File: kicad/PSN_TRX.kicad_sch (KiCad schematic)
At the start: 164 parts, among them IC1 LP2950L-5.0V, IC2 NJM2904, J1 PWR_IN, J2 PWR_IN, J3 PWR_IN, J4 MIC-IN, J5 FREQ-VC, J6 Volume, K1 G5V-2, Q1 3SK59, Q10 2SK439, Q11 2SC1815, Q12 2SC1815, Q13 2SC1815, Q14 2SK439, Q15 2SC1815, Q17 2SC1815, Q2 2SC1923, Q3 2SC1815, Q4 2SC1815, Q5 2SC2120, Q6 2SA950, Q7 2SC1923, Q8 2SC1923, Q9 2SK439, SW1 SW, SW2 SW, T1 ST-71, X1 50.5MHz/3

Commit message: Arduino Nano R4 移植 & KiCad ライブラリ統合
- Arduino Nano R4 (Renesas RA4M1) への移植完了
  * スケッチ: ESP32 → Nano R4 対応に変更
  * GPIO ピン: 再割り当て (GPIO21/22 → A4/A5 など)
  * ストレージ: Preferences → EEPROM に変更
  * リポジトリ名: PSN_TRX_ESP32 → PSN_TRX_Nano_R4

- KiCad シンボル・フットプリント作成
  * Arduino_Nano_R4_Socket (DIP 30)
  * Si5351A (QFN-20)
  * Si5351_DIP8 モジュール (DIP 8)
  * すべてピン位置を 2.54mm グリッドに整列

- ライブラリ統合
  * sym-lib-table に 4 つのシンボルライブラリ登録
  * fp-lib-table に フットプリント登録
  * 絶対パスに統一

- ドキュメント更新
  * PSN_TRX_VFO改造仕様書.docx に全変更内容を記録
  * ピン配置表、ライブラリ情報を追加

- VXO 回路変更
  * VXO 部分を別の回路に変更

Co-Authored-By: Claude Haiku 4.5 <noreply@anthropic.com>
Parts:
- removed C10, C9: 100p, Capacitor_THT:C_Disc_D3.0mm_W1.6mm_P2.50mm, symbol Device:C
- removed C11, C12, C14: 47p, Capacitor_THT:C_Disc_D3.0mm_W1.6mm_P2.50mm, symbol Device:C
- removed C112: 0.01u, Capacitor_THT:C_Disc_D5.0mm_W2.5mm_P2.50mm, symbol Device:C
- removed C13: 5p, Capacitor_THT:C_Disc_D3.0mm_W1.6mm_P2.50mm, symbol Device:C
- removed C18: 15p, Capacitor_THT:C_Disc_D3.0mm_W1.6mm_P2.50mm, symbol Device:C
- removed C19, C20: 33p, Capacitor_THT:C_Disc_D3.0mm_W1.6mm_P2.50mm, symbol Device:C
- removed J5: FREQ-VC, Connector_PinHeader_2.54mm:PinHeader_1x02_P2.54mm_Vertical, symbol Connector_Generic:Conn_01x02
- removed L3: 7T5, PSN_TRX:L_FCZ07S_CT, symbol PSN_TRX:L_7T50_CT
- removed L4: T-30-10 6T/0.4mm, PSN_TRX:L_T30_2pin_Vertical, symbol Device:L
- removed L5: T-30-10 6T+1T/0.4mm, PSN_TRX:L_T30_3pin_Vertical, symbol Device:Transformer_1P_1S
- removed L7: 7T50, PSN_TRX:L_FCZ07S_CT, symbol PSN_TRX:L_7T50_CT
- removed Q10: 2SK439, Package_TO_SOT_THT:TO-92_Inline, symbol Device:Q_NMOS
- removed Q7, Q8: 2SC1923, Package_TO_SOT_THT:TO-92_Inline, symbol Transistor_BJT:Q_NPN_BCE
- removed R16: 10k, Resistor_THT:R_Axial_DIN0207_L6.3mm_D2.5mm_P2.54mm_Vertical, symbol Device:R
- removed R17, R20: 100k, Resistor_THT:R_Axial_DIN0207_L6.3mm_D2.5mm_P2.54mm_Vertical, symbol Device:R
- removed R18: 1k, Resistor_THT:R_Axial_DIN0207_L6.3mm_D2.5mm_P2.54mm_Vertical, symbol Device:R
- removed R44: 100, Resistor_THT:R_Axial_DIN0207_L6.3mm_D2.5mm_P2.54mm_Vertical, symbol Device:R
- removed TC1, TC2: 40p, PSN_TRX:C_Trimmer_TMCV01, symbol Device:C_Variable
- removed VC1: 30p, PSN_TRX:C_Trimmer_TMCV01, symbol Device:C_Variable
- removed X1: 50.5MHz/3, Crystal:Crystal_HC49-4H_Vertical, symbol Device:Crystal
- added A1: Arduino_Nano_R4_Socket, PSN_TRX:Arduino_Nano_R4_Socket, symbol Arduino_Nano_R4:Arduino_Nano_R4_Socket
- added C128, C129, C130, C131: 47PF, Capacitor_THT:C_Disc_D5.0mm_W2.5mm_P2.50mm, symbol Device:C
- added L16, L17: 100nH, PSN_TRX:L_AL0510-153K_Vertical, symbol Device:L
- added U1: Si5351_DIP8, PSN_TRX:DIP-8_W7.62mm, symbol Si5351_DIP8:Si5351_DIP8
- added VR6, VR7: 500, Potentiometer_THT:Potentiometer_Alps_RK09K_Single_Vertical, symbol Device:R_Potentiometer
- R21: value 220k -> 47
- R34: value 100 -> 47
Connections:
- net +5V: now also A1.30 (VIN), U1.8 (VDD); no longer C115.1, R21.2
- net GND: now also R21.2, A1.18 (GND), A1.28 (GND), A1.29 (GND), C128.1, C129.1, C130.1, C131.1, U1.4 (GND); no longer C115.2, C116.2
- net at R21.1: now also C114.2, C21.1, VR6.1
- net at C116.1: now also C131.2, L17.1
- net at R34.1: now also C22.1, VR7.1; no longer C21.1
- new net: C115.1, C128.2, L16.1
- new net: C129.2, L16.2, VR6.2, VR6.3
- new net: C130.2, L17.2, VR7.2, VR7.3
- new net: C115.2, U1.5 (CLK0)
- new net: A1.21 (A5/SCL), U1.2 (SCL)
- new net: A1.22 (A4/SDA), U1.3 (SDA)
- new net: C116.2, U1.6 (CLK1)
- no-connect marks 9 -> 30
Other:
- note added: "DDS"
- note removed: "VXO"
- moved on the sheet: C1, C100, C101, C102, C103, C104, C105, C111, C113, C114, C117, C118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

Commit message: J5 I2C_OUT コネクタ（3ピン）を追加
- Arduino Nano R4 の A4（SDA）、A5（SCL）から I2C 出力コネクタを実装
- J5: 3ピンコネクタ（SDA/SCL/GND）
- フットプリント: Connector_PinHeader_2.54mm:PinHeader_1x03_P2.54mm_Vertical
- シンボル: PSN_TRX:I2C_OUT カスタムシンボル
- スケマティクスに配線完了

Co-Authored-By: Claude Haiku 4.5 <noreply@anthropic.com>
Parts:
- added J5: Conn_01x03_MountingPin, Connector_PinHeader_2.54mm:PinHeader_1x03_P2.54mm_Vertical, symbol Connector_Generic_MountingPin:Conn_01x03_MountingPin
- added J5: I2C_OUT, Connector_PinHeader_2.54mm:PinHeader_1x03_P2.54mm_Vertical, symbol PSN_TRX:I2C_OUT
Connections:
- net GND: now also J5.3 (Pin_3)
- net at A1.21 (A5/SCL), U1.2 (SCL): now also J5.2 (Pin_2)
- net at A1.22 (A4/SDA), U1.3 (SDA): now also J5.1 (Pin_1)

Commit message: スケマティクス更新（KiCad 再起動後の反映）
- J5 I2C_OUT シンボル表示を PSN_TRX:I2C_OUT に更新
- キャッシュクリア後の最終確認

Co-Authored-By: Claude Haiku 4.5 <noreply@anthropic.com>
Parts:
- removed J5: Conn_01x03_MountingPin, Connector_PinHeader_2.54mm:PinHeader_1x03_P2.54mm_Vertical, symbol Connector_Generic_MountingPin:Conn_01x03_MountingPin
- added J5: I2C_OUT, Connector_PinHeader_2.54mm:PinHeader_1x03_P2.54mm_Vertical, symbol PSN_TRX:I2C_OUT
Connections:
- net GND: now also J5.3 (GND)
- net at A1.22 (A4/SDA), U1.3 (SDA): now also J5.1 (SDA)
- net at A1.21 (A5/SCL), U1.2 (SCL): now also J5.2 (SCL)
- no-connect marks 30 -> 31
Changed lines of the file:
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@@
 	)
 	(no_connect
+		(at 690.88 318.77)
+	)
+	(no_connect
 		(at 671.83 336.55)
 	)
@@
 	)
 	(symbol
+		(lib_id "PSN_TRX:I2C_OUT")
+		(at 744.22 383.54 0)
+		(unit 1)
+		(body_style 1)
+		(exclude_from_sim no)
+		(in_bom yes)
+		(on_board yes)
+		(in_pos_files yes)
+		(dnp no)
+		(property "Reference" "J5"
+			(at 751.84 382.524 0)
+			(show_name no)
+			(do_not_autoplace no)
+			(effects
+				(font
+					(size 1.27 1.27)
+					(thickness 0.15)
+				)
+				(justify left)
+			)
+		)
+		(property "Value" "I2C_OUT"
+			(at 751.332 385.064 0)
+			(show_name no)
+			(do_not_autoplace no)
+			(effects
+				(font
+					(size 1.27 1.27)
+					(thickness 0.15)
+				)
+				(justify left)
+			)
+		)
+		(property "Footprint" "Connector_PinHeader_2.54mm:PinHeader_1x03_P2.54mm_Vertical"
+			(at 744.22 383.54 0)
+			(hide yes)
+			(show_name no)
+			(do_not_autoplace no)
+			(effects
+				(font
+					(size 1.27 1.27)
+					(thickness 0.15)
+				)
+			)
+		)
+		(property "Datasheet" ""
+			(at 744.22 383.54 0)
+			(hide yes)
+			(show_name no)
+			(do_not_autoplace no)
+			(effects
+				(font
+					(size 1.27 1.27)
+					(thickness 0.15)
+				)
+			)
+		)
+		(property "Description" "I2C output connector, 3-pin header, Pin1=SDA, Pin2=SCL, Pin3=GND"
+			(at 744.22 383.54 0)
+			(hide yes)
+			(show_name no)
+			(do_not_autoplace no)
+			(effects
+				(font
+					(size 1.27 1.27)
+				)
+			)
+		)
+		(pin "1"
+		)
+		(pin "2"
+		)
+		(pin "3"
+		)
+		(instances
+			(project "PSN_TRX"
+				(path "/50835569-93ad-4c8c-aafc-424a6a3761ef"
+					(reference "J5")
+					(unit 1)
+				)
+			)
+		)
+	)
+	(symbol
 		(lib_id "Device:C")
 		(at 396.24 327.66 0)
@@
 					(unit 1)
 				)
-			)
-		)
-	)
-	(symbol
-		(lib_id "Connector_Generic_MountingPin:Conn_01x03_MountingPin")
-		(at 744.22 384.81 0)
-		(unit 1)
-		(body_style 1)
-		(exclude_from_sim no)
-		(in_bom yes)
-		(on_board yes)
-		(in_pos_files yes)
-		(dnp no)
-		(fields_autoplaced yes)
-		(property "Reference" "J5"
-			(at 746.76 383.8955 0)
-			(show_name no)
-			(do_not_autoplace no)
-			(effects
-				(font
-					(size 1.27 1.27)
-				)
-				(justify left)
-			)
-		)
-		(property "Value" "Conn_01x03_MountingPin"
-			(at 746.76 386.4355 0)
-			(show_name no)
-			(do_not_autoplace no)
-			(effects
-				(font
-					(size 1.27 1.27)
-				)
-				(justify left)
-			)
-		)
-		(property "Footprint" "Connector_PinHeader_2.54mm:PinHeader_1x03_P2.54mm_Vertical"
-			(at 744.22 384.81 0)
-			(hide yes)
-			(show_name no)
-			(do_not_autoplace no)
-			(effects
-				(font
-					(size 1.27 1.27)
-				)
-			)
-		)
-		(property "Datasheet" ""
-			(at 744.22 384.81 0)
-			(hide yes)
-			(show_name no)
-			(do_not_autoplace no)
-			(effects
-				(font
-					(size 1.27 1.27)
-				)
-			)
-		)
-		(property "Description" "Generic connectable mounting pin connector, single row, 01x03, script generated (kicad-library-utils/schlib/autogen/connector/)"
-			(at 744.22 384.81 0)
-			(hide yes)
-			(show_name no)
-			(do_not_autoplace no)
-			(effects
-				(font
-					(size 1.27 1.27)
-				)
-			)
-		)
-		(pin "3"
-		)
-		(pin "2"
-		)
-		(pin "1"
-		)
-		(pin "MP"
-		)
-		(instances
-			(project "PSN_TRX"
-				(path "/50835569-93ad-4c8c-aafc-424a6a3761ef"
-					(reference "J5")
-					(unit 1)
-				)

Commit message: Fix library paths for macOS compatibility
Windows絶対パスを${KIPRJMOD}相対パスに変更。
未使用のArduino外部ライブラリエントリを削除。

Co-Authored-By: Claude Sonnet 4.6 <noreply@anthropic.com>
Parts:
- removed J5: I2C_OUT, Connector_PinHeader_2.54mm:PinHeader_1x03_P2.54mm_Vertical, symbol PSN_TRX:I2C_OUT
- J2: value PWR_IN -> SP-OUT
- J3: value PWR_IN -> RF-IN
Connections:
- net +5V: no longer K1.1
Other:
- moved on the sheet: C111, C113, C114, C120, C124, C17, C21, C22, C23, C8, C8b1, D1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

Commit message: Update schematic (KiCad auto-modified junctions)
Co-Authored-By: Claude Sonnet 4.6 <noreply@anthropic.com>
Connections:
- net +5V: now also K1.1
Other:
- moved on the sheet: C3, C8, C8b1, IC1, J1, J3, K1, LED1, R13, SW1, SW2

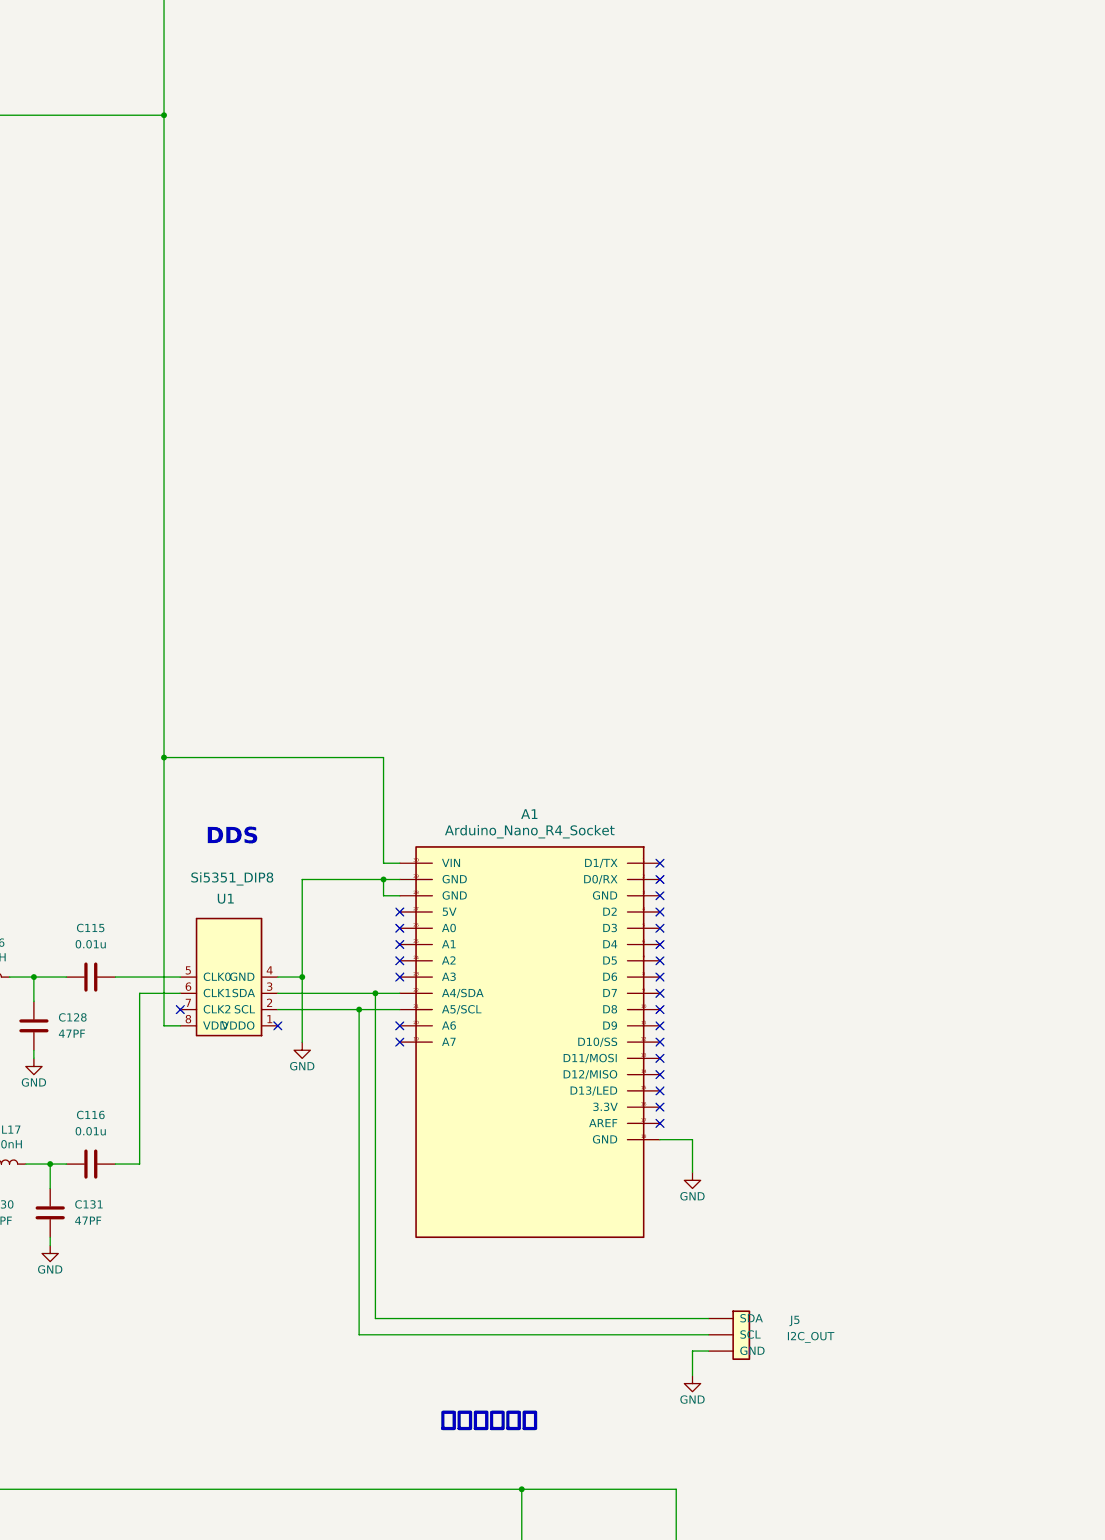
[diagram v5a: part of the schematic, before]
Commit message: KiCadシンボル・フットプリント追加、ERC修正
- AE_LCNV4_MOSFET.kicad_sym 新規作成（秋月AE-LCNV4-MOSFET 4chレベルシフタ）
- DIP-12_W7.62mm.kicad_mod 新規作成（DIP-12フットプリント）
- sym-lib-table に AE_LCNV4_MOSFET ライブラリ登録
- Si5351_DIP8 VDD(8番)ピンを power_in → passive に変更（ERC修正）
- AE-LCNV4-MOSFET HV(4番)/GND(3,10番)/LV(9番)を power_in → passive に変更（ERC修正）
- Arduino_Nano_R4_Socket 3.3V(16番)ピンを passive → power_out に変更

Co-Authored-By: Claude Sonnet 4.6 <noreply@anthropic.com>
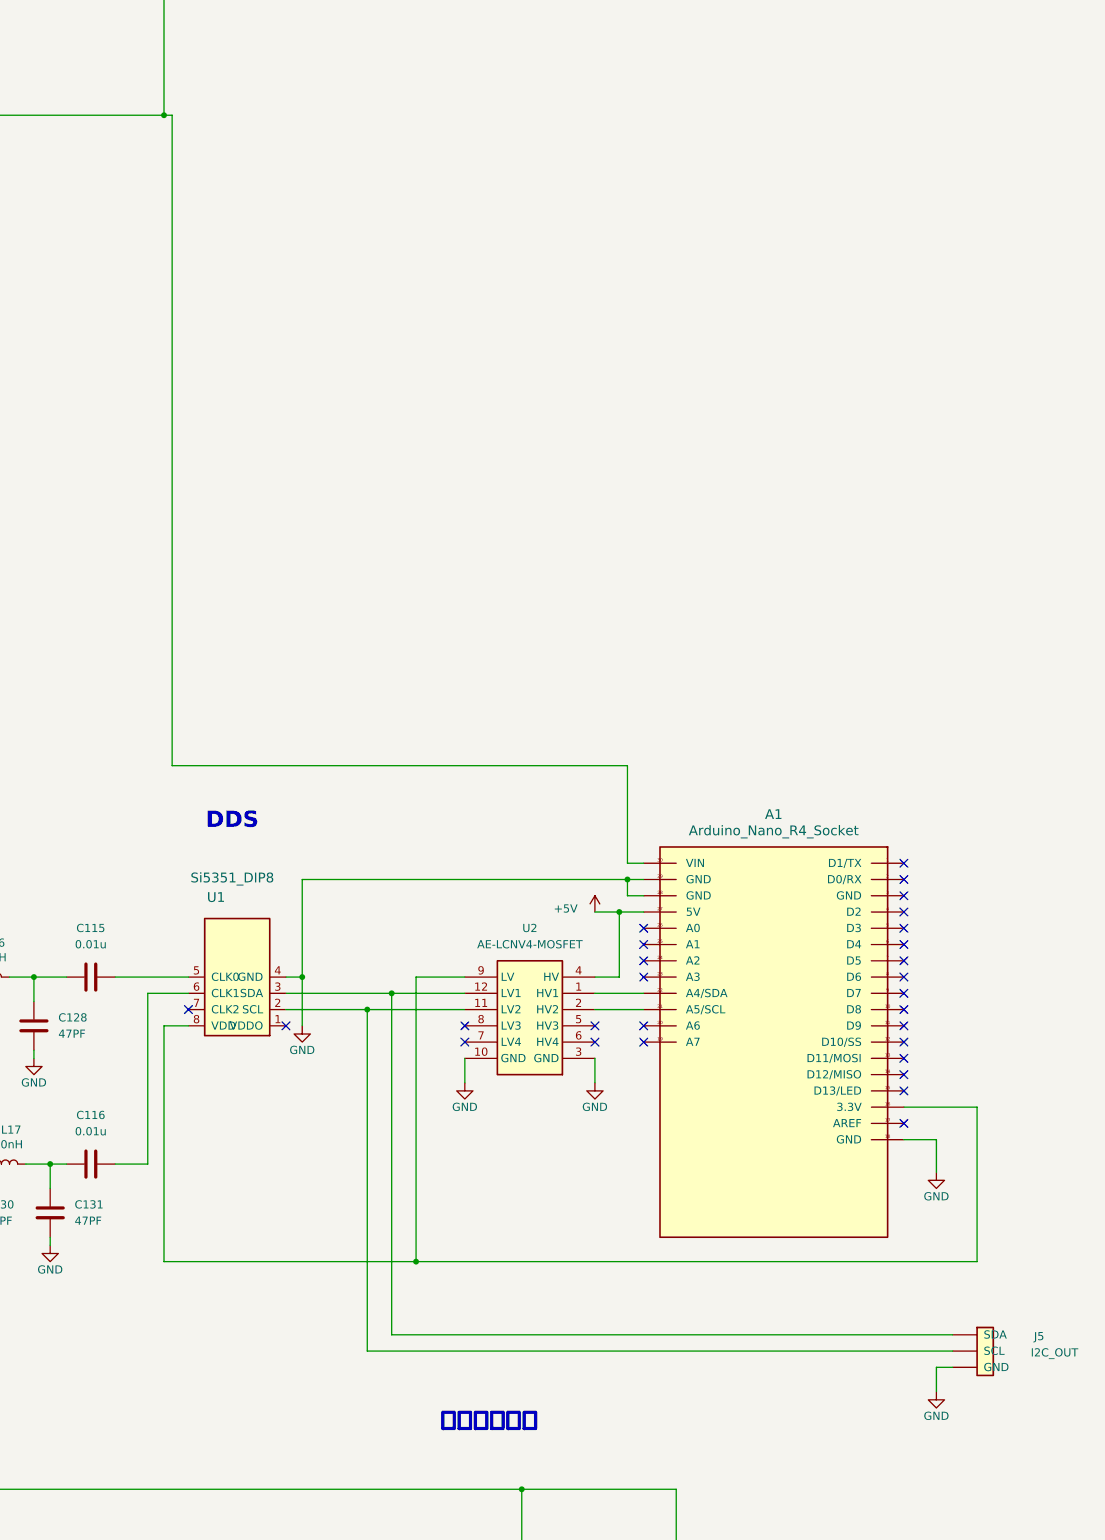
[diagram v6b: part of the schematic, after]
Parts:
- added U2: AE-LCNV4-MOSFET, PSN_TRX:DIP-12_W7.62mm, symbol AE_LCNV4_MOSFET:AE-LCNV4-MOSFET
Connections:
- net +5V: now also A1.27 (5V), U2.4 (HV); no longer U1.8 (VDD)
- net GND: now also U2.10 (GND), U2.3 (GND)
- net at J5.1 (SDA), U1.3 (SDA): now also U2.12 (LV1); no longer A1.22 (A4/SDA)
- net at J5.2 (SCL), U1.2 (SCL): now also U2.11 (LV2); no longer A1.21 (A5/SCL)
- net at A1.16 (3.3V): now also U1.8 (VDD), U2.9 (LV)
- new net: A1.21 (A5/SCL), U2.2 (HV2)
- new net: A1.22 (A4/SDA), U2.1 (HV1)
- no-connect marks 31 -> 33
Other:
- moved on the sheet: A1, J5

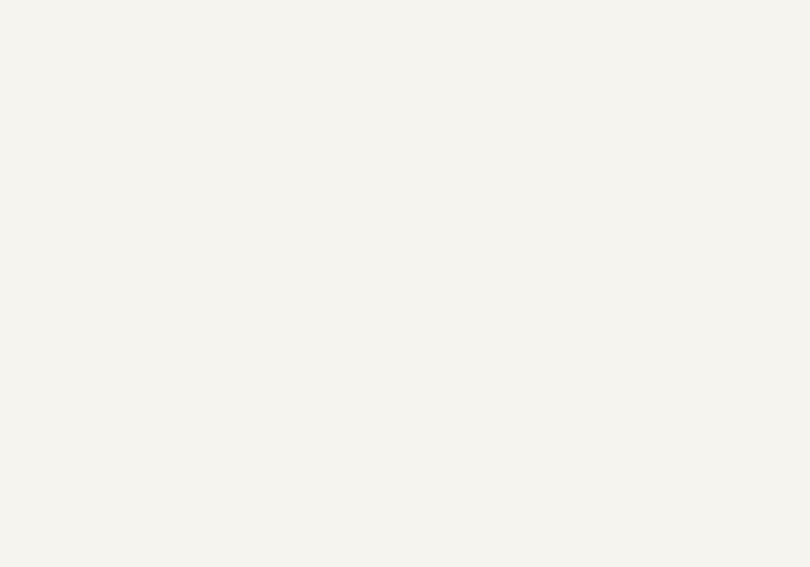
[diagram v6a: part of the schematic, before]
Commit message: KiCad: シンボル統合・パネル部品除外・PCBクリーンアップ
- 外部シンボルファイル4本をPSN_TRX.kicad_symに統合
  (Arduino_Nano_R4_Socket, Si5351_DIP8, Si5351A, AE-LCNV4-MOSFET)
  → sym-lib-tableはPSN_TRXライブラリのみに統一
- SW1, SW2, R13, LED1をon_board=noに変更（パネル取付部品）
- PCBからSW1, R13, LED1フットプリントを削除（SW2は元から未配置）
- .gitignoreに_restore_backup_*/を追加

Co-Authored-By: Claude Sonnet 4.6 <noreply@anthropic.com>
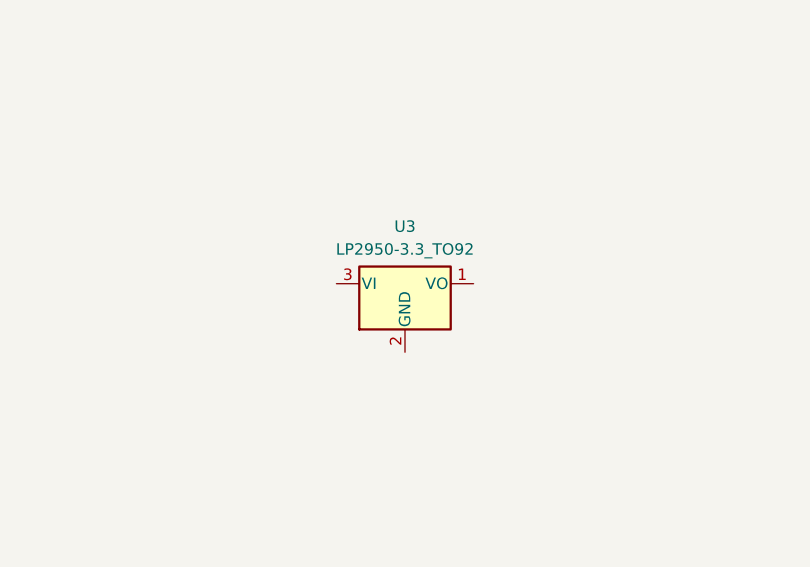
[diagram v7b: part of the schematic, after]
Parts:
- added U3: LP2950-3.3_TO92, Package_TO_SOT_THT:TO-92_Inline, symbol Regulator_Linear:LP2950-3.3_TO92
- A1: symbol Arduino_Nano_R4:Arduino_Nano_R4_Socket -> PSN_TRX:Arduino_Nano_R4_Socket
- U1: symbol Si5351_DIP8:Si5351_DIP8 -> PSN_TRX:Si5351_DIP8
- U2: symbol AE_LCNV4_MOSFET:AE-LCNV4-MOSFET -> PSN_TRX:AE-LCNV4-MOSFET
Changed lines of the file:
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@@
 	)
 	(symbol
-		(lib_id "Arduino_Nano_R4:Arduino_Nano_R4_Socket")
+		(lib_id "PSN_TRX:Arduino_Nano_R4_Socket")
 		(at 749.3 339.09 0)
 		(mirror y)
@@
 	)
 	(symbol
-		(lib_id "AE_LCNV4_MOSFET:AE-LCNV4-MOSFET")
+		(lib_id "Regulator_Linear:LP2950-3.3_TO92")
+		(at 711.2 226.06 0)
+		(unit 1)
+		(body_style 1)
+		(exclude_from_sim no)
+		(in_bom yes)
+		(on_board yes)
+		(in_pos_files yes)
+		(dnp no)
+		(fields_autoplaced yes)
+		(property "Reference" "U3"
+			(at 711.2 219.71 0)
+			(show_name no)
+			(do_not_autoplace no)
+			(effects
+				(font
+					(size 1.27 1.27)
+				)
+			)
+		)
+		(property "Value" "LP2950-3.3_TO92"
+			(at 711.2 222.25 0)
+			(show_name no)
+			(do_not_autoplace no)
+			(effects
+				(font
+					(size 1.27 1.27)
+				)
+			)
+		)
+		(property "Footprint" "Package_TO_SOT_THT:TO-92_Inline"
+			(at 711.2 220.345 0)
+			(hide yes)
+			(show_name no)
+			(do_not_autoplace no)
+			(effects
+				(font
+					(size 1.27 1.27)
+					(italic yes)
+				)
+			)
+		)
+		(property "Datasheet" "http://www.ti.com/lit/ds/symlink/lp2950.pdf"
+			(at 711.2 227.33 0)
+			(hide yes)
+			(show_name no)
+			(do_not_autoplace no)
+			(effects
+				(font
+					(size 1.27 1.27)
+				)
+			)
+		)
+		(property "Description" "Positive 100mA 30V Linear Micropower Voltage Regulator, Fixed Output 3.3V, TO-92"
+			(at 711.2 226.06 0)
+			(hide yes)
+			(show_name no)
+			(do_not_autoplace no)
+			(effects
+				(font
+					(size 1.27 1.27)
+				)
+			)
+		)
+		(pin "2"
+		)
+		(pin "1"
+		)
+		(pin "3"
+		)
+		(instances
+			(project "PSN_TRX"
+				(path "/50835569-93ad-4c8c-aafc-424a6a3761ef"
+					(reference "U3")
+					(unit 1)
+				)
+			)
+		)
+	)
+	(symbol
+		(lib_id "PSN_TRX:AE-LCNV4-MOSFET")
 		(at 711.2 335.28 0)
 		(mirror y)
@@
 		(exclude_from_sim no)
 		(in_bom yes)
-		(on_board yes)
+		(on_board no)
 		(in_pos_files yes)
 		(dnp no)
@@
 	)
 	(symbol
-		(lib_id "Si5351_DIP8:Si5351_DIP8")
+		(lib_id "PSN_TRX:Si5351_DIP8")
 		(at 665.48 328.93 180)
 		(unit 1)
@@
 		(exclude_from_sim no)
 		(in_bom yes)
-		(on_board yes)
+		(on_board no)
 		(in_pos_files yes)
 		(dnp no)
@@
 		(exclude_from_sim no)
 		(in_bom yes)
-		(on_board yes)
+		(on_board no)
 		(in_pos_files yes)
 		(dnp no)
@@
 		(exclude_from_sim no)
 		(in_bom yes)
-		(on_board yes)
+		(on_board no)
 		(in_pos_files yes)
 		(dnp no)
